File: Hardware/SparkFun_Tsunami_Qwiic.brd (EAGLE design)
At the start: 74.9 x 73.7 mm, 327 parts, among them J1 VDC-IN, J10 TRIG2, J11 TRIG1, J14 AUDIO I/O, J15 MIDI, J16 USB-C, J17 AGND, J2 GND-IN, J3 DEBUG, J4 QWIIC, J6 3.3VA, J7 3.3V, J8 PLAYING, J9 CORTEX_JTAG_DEBUG_PTH_NS, Q1 3.1A/30V/105mΩ, U1 LM1117, U3 ATSAMS70N20A-AN, U4 LMV324, U5 LM1117, U6 6N138M, U7 ADAU1328, U8 SN74AHC1G125, Y1 11.2896 MHz

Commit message: Single buffer gate change
drop in replacement for U8 single buffer IC, with new PROD_ID
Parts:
- U8: value SN74AHC1G125 -> 74AHC1G125W5-7
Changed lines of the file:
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@@
 <setting verticaltext="up"/>
 </settings>
-<grid distance="0.05" unitdist="inch" unit="inch" style="lines" multiple="1" display="yes" altdistance="0.001" altunitdist="inch" altunit="inch"/>
+<grid distance="0.05" unitdist="inch" unit="inch" style="lines" multiple="1" display="yes" altdistance="0.005" altunitdist="inch" altunit="inch"/>
 <layers>
 <layer number="1" name="Top" color="4" fill="1" visible="yes" active="yes"/>
@@
 <layer number="98" name="Guide" color="6" fill="1" visible="no" active="no"/>
 <layer number="99" name="SpiceOrder" color="7" fill="1" visible="no" active="no"/>
-<layer number="100" name="Muster" color="7" fill="1" visible="no" active="no"/>
+<layer number="100" name="Muster" color="7" fill="1" visible="no" active="yes"/>
 <layer number="101" name="Patch_Top" color="12" fill="4" visible="no" active="yes"/>
 <layer number="102" name="Vscore" color="7" fill="1" visible="no" active="yes"/>
@@
 <element name="U$94" library="output2" package="CIPO23" value="" x="39.375078125" y="40.15231875" smashed="yes" rot="MR270"/>
 <element name="U$95" library="output2" package="APDM26" value="" x="31.755078125" y="40.15231875" smashed="yes" rot="MR270"/>
-<element name="U8" library="SparkFun-IC-Logic" package="SOT23-5" value="SN74AHC1G125" x="26.416" y="59.944" smashed="yes">
+<element name="U8" library="SparkFun-IC-Logic" package="SOT23-5" value="74AHC1G125W5-7" x="26.416" y="59.944" smashed="yes">
 <attribute name="NAME" x="24.511" y="59.944" size="0.6096" layer="25" font="vector" ratio="20" rot="R90" align="bottom-center"/>
-<attribute name="PROD_ID" value="IC-11920" x="26.416" y="59.944" size="1.778" layer="27" font="vector" ratio="15" display="off"/>
-<attribute name="VALUE" x="28.956" y="59.944" size="0.6096" layer="27" font="vector" ratio="20" rot="R90" align="bottom-center"/>
+<attribute name="PROD_ID" value="IC-16588" x="26.416" y="59.944" size="1.778" layer="27" font="vector" ratio="15" display="off"/>
+<attribute name="VALUE" value="74AHC1G125W5-7" x="28.956" y="59.944" size="0.6096" layer="27" font="vector" ratio="20" rot="R90" align="bottom-center"/>
 </element>
 <element name="U5" library="SparkFun-IC-Power" package="SOT223" value="LM1117" x="53.34" y="40.386" smashed="yes" rot="R270">

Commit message: Swap 11MHz crystal for smaller package (3.2x2.5mm)
-also bumped version in bottom copper and SCH
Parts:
- Y1: device SparkFun-Clocks:CRYSTAL-OSC-SMD-5X3 -> SparkFun-Clocks:CRYSTAL-SMD-3.2X2.5MM_GEYER_12.60421
- moved C7 0.85 mm to (39.8, 22.2)
- moved C9 0.72 mm to (39.0, 28.6)
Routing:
- net N$1: track 10.0 -> 8.21 mm
- net N$2: track 6.94 -> 6.21 mm
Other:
- board text added: "V22"
- board text removed: "V21"
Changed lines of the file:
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@@
 <setting verticaltext="up"/>
 </settings>
-<grid distance="0.05" unitdist="inch" unit="inch" style="lines" multiple="1" display="yes" altdistance="0.005" altunitdist="inch" altunit="inch"/>
+<grid distance="0.05" unitdist="inch" unit="inch" style="lines" multiple="1" display="yes" altdistance="0.001" altunitdist="inch" altunit="inch"/>
 <layers>
 <layer number="1" name="Top" color="4" fill="1" visible="yes" active="yes"/>
@@
 <layer number="98" name="Guide" color="6" fill="1" visible="no" active="no"/>
 <layer number="99" name="SpiceOrder" color="7" fill="1" visible="no" active="no"/>
-<layer number="100" name="Muster" color="7" fill="1" visible="no" active="yes"/>
+<layer number="100" name="Muster" color="7" fill="1" visible="yes" active="yes"/>
 <layer number="101" name="Patch_Top" color="12" fill="4" visible="no" active="yes"/>
 <layer number="102" name="Vscore" color="7" fill="1" visible="no" active="yes"/>
@@
 <wire x1="0" y1="73.66" x2="0" y2="0" width="0.2032" layer="20"/>
 <text x="29.21" y="-31.75" size="1.778" layer="51" font="vector">Jamie Robertson &amp; Byron Jacquot</text>
-<text x="32.90061875" y="73.2663" size="1.778" layer="16" font="vector" ratio="15" rot="SMR180">V21</text>
+<text x="32.90061875" y="73.2663" size="1.778" layer="16" font="vector" ratio="15" rot="SMR180">V22</text>
 <wire x1="67.31" y1="71.12" x2="64.081659375" y2="71.137778125" width="0.2032" layer="21"/>
 <wire x1="63.573659375" y1="70.629778125" x2="64.081659375" y2="71.137778125" width="0.2032" layer="21"/>
@@
 <attribute name="REV" value="" x="-1.27" y="-31.75" size="1.778" layer="27" display="off"/>
 </element>
-<element name="C9" library="SparkFun-Capacitors" package="0402-TIGHT" value="12pF" x="38.686740625" y="29.220159375" smashed="yes">
-<attribute name="NAME" x="37.797740625" y="29.982159375" size="0.4064" layer="25" font="vector"/>
-<attribute name="PROD_ID" value="CAP-14665" x="38.686740625" y="29.220159375" size="1.778" layer="27" display="off"/>
-<attribute name="VALUE" x="37.670740625" y="28.077159375" size="0.4064" layer="27" font="vector"/>
-</element>
-<element name="C7" library="SparkFun-Capacitors" package="0402-TIGHT" value="12pF" x="39.22268125" y="21.529040625" smashed="yes" rot="R180">
-<attribute name="NAME" x="40.11168125" y="20.767040625" size="0.4064" layer="25" font="vector" rot="R180"/>
-<attribute name="PROD_ID" value="CAP-14665" x="39.22268125" y="21.529040625" size="1.778" layer="27" rot="R180" display="off"/>
-<attribute name="VALUE" x="40.23868125" y="22.672040625" size="0.4064" layer="27" font="vector" rot="R180"/>
+<element name="C9" library="SparkFun-Capacitors" package="0402-TIGHT" value="12pF" x="38.966140625" y="28.559759375" smashed="yes">
+<attribute name="NAME" x="38.077140625" y="29.321759375" size="0.4064" layer="25" font="vector"/>
+<attribute name="PROD_ID" value="CAP-14665" x="38.966140625" y="28.559759375" size="1.778" layer="27" display="off"/>
+<attribute name="VALUE" x="37.950140625" y="27.416759375" size="0.4064" layer="27" font="vector"/>
+</element>
+<element name="C7" library="SparkFun-Capacitors" package="0402-TIGHT" value="12pF" x="39.75608125" y="22.189440625" smashed="yes" rot="R180">
+<attribute name="NAME" x="40.64508125" y="21.427440625" size="0.4064" layer="25" font="vector" rot="R180"/>
+<attribute name="PROD_ID" value="CAP-14665" x="39.75608125" y="22.189440625" size="1.778" layer="27" rot="R180" display="off"/>
+<attribute name="VALUE" x="40.77208125" y="23.332440625" size="0.4064" layer="27" font="vector" rot="R180"/>
 </element>
 <element name="FB1" library="SparkFun-Coils" package="0603" value="470Ω" x="34.79291875" y="32.390078125" smashed="yes" rot="R270">
@@
 <attribute name="VALUE" value="0.1uF" x="61.468" y="51.054" size="0.4064" layer="27" font="vector" rot="R180"/>
 </element>
-<element name="Y1" library="SparkFun-Clocks" package="CRYSTAL-OSC-SMD-5X3" value="11.2896 MHz" x="39.37" y="25.4" smashed="yes" rot="R90">
-<attribute name="DKPART" value="887-2353-1-ND" x="39.37" y="25.4" size="1.778" layer="27" font="vector" ratio="15" rot="R90" display="off"/>
-<attribute name="MFR" value="txc" x="39.37" y="25.4" size="1.778" layer="27" font="vector" ratio="15" rot="R90" display="off"/>
-<attribute name="MFRPART" value="7B-11.2896MAAE-T" x="39.37" y="25.4" size="1.778" layer="27" font="vector" ratio="15" rot="R90" display="off"/>
+<element name="Y1" library="SparkFun-Clocks" package="CRYSTAL-SMD-3.2X2.5MM_GEYER_12.60421" value="11.2896 MHz" x="39.37" y="25.4" smashed="yes" rot="R90">
+<attribute name="MFR" value="GEYER" x="39.37" y="25.4" size="1.778" layer="27" font="vector" ratio="15" rot="R90" display="off"/>
+<attribute name="MODEL" value="KX-7T" x="39.37" y="25.4" size="1.778" layer="27" rot="R90" display="off"/>
+<attribute name="MRFPART" value="12.60421" x="39.37" y="25.4" size="1.778" layer="27" rot="R90" display="off"/>
 <attribute name="NAME" x="37.465" y="22.86" size="0.4064" layer="25" rot="R90"/>
-<attribute name="PROD_ID" value="XTAL-13463" x="39.37" y="25.4" size="1.778" layer="27" rot="R90" display="off"/>
+<attribute name="PROD_ID" value="XTAL-16991" x="39.37" y="25.4" size="1.778" layer="27" rot="R90" display="off"/>
 <attribute name="VALUE" x="41.91" y="22.86" size="0.4064" layer="27" rot="R90"/>
 </element>
@@
 <contactref element="C7" pad="1"/>
 <contactref element="U3" pad="98"/>
-<wire x1="34.57" y1="25.32" x2="39.958" y2="25.32" width="0.2032" layer="1"/>
-<wire x1="39.958" y1="25.32" x2="40.52" y2="24.758" width="0.2032" layer="1"/>
 <contactref element="Y1" pad="1"/>
-<wire x1="40.52" y1="23.55" x2="40.52" y2="24.758" width="0.2032" layer="1"/>
-<wire x1="39.72268125" y1="21.529040625" x2="40.23068125" y2="21.529040625" width="0.2032" layer="1"/>
-<wire x1="40.52" y1="21.818359375" x2="40.23068125" y2="21.529040625" width="0.2032" layer="1"/>
-<wire x1="40.52" y1="21.818359375" x2="40.52" y2="23.55" width="0.2032" layer="1"/>
+<wire x1="40.25608125" y1="22.189440625" x2="40.25608125" y2="24.23608125" width="0.2032" layer="1"/>
+<wire x1="40.25608125" y1="24.23608125" x2="40.27" y2="24.25" width="0.2032" layer="1"/>
+<wire x1="34.57" y1="25.32" x2="39.2" y2="25.32" width="0.2032" layer="1"/>
+<wire x1="39.2" y1="25.32" x2="40.27" y2="24.25" width="0.2032" layer="1"/>
 </signal>
 <signal name="N$2">
 <contactref element="C9" pad="1"/>
 <contactref element="U3" pad="99"/>
-<wire x1="34.57" y1="25.82" x2="38.012" y2="25.82" width="0.2032" layer="1"/>
 <contactref element="Y1" pad="3"/>
-<wire x1="38.22" y1="27.25" x2="38.22" y2="26.028" width="0.2032" layer="1"/>
-<wire x1="38.22" y1="26.028" x2="38.012" y2="25.82" width="0.2032" layer="1"/>
-<wire x1="38.186740625" y1="29.220159375" x2="38.186740625" y2="27.283259375" width="0.2032" layer="1"/>
-<wire x1="38.186740625" y1="27.283259375" x2="38.22" y2="27.25" width="0.2032" layer="1"/>
+<wire x1="38.47" y1="26.55" x2="38.466140625" y2="26.553859375" width="0.2032" layer="1"/>
+<wire x1="38.466140625" y1="26.553859375" x2="38.466140625" y2="28.559759375" width="0.2032" layer="1"/>
+<wire x1="34.57" y1="25.82" x2="37.74" y2="25.82" width="0.2032" layer="1"/>
+<wire x1="37.74" y1="25.82" x2="38.47" y2="26.55" width="0.2032" layer="1"/>
 </signal>
 <signal name="N$3">

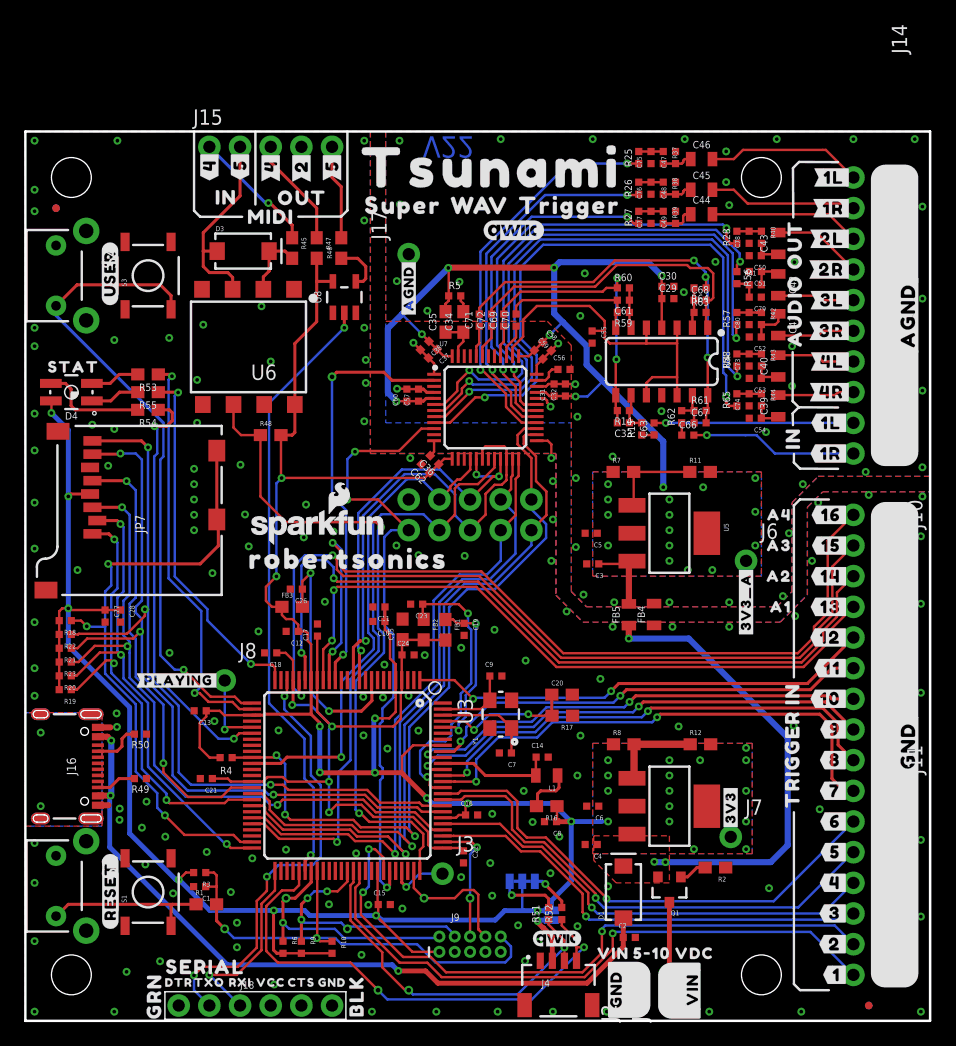
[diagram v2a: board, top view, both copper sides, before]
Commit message: Test points changed to larger size
-8 test points updated. Note, these used to be the small 15mil drill hit pth/via style test points. They are now the largest SMD pad style. Note, I also kept a via in the center point of all the test points, this was necessary to keep routing adjustments to a minimum and it will also help with pogo pin centering.
-Bumped version to v23 in BRD and both sheets of SCH
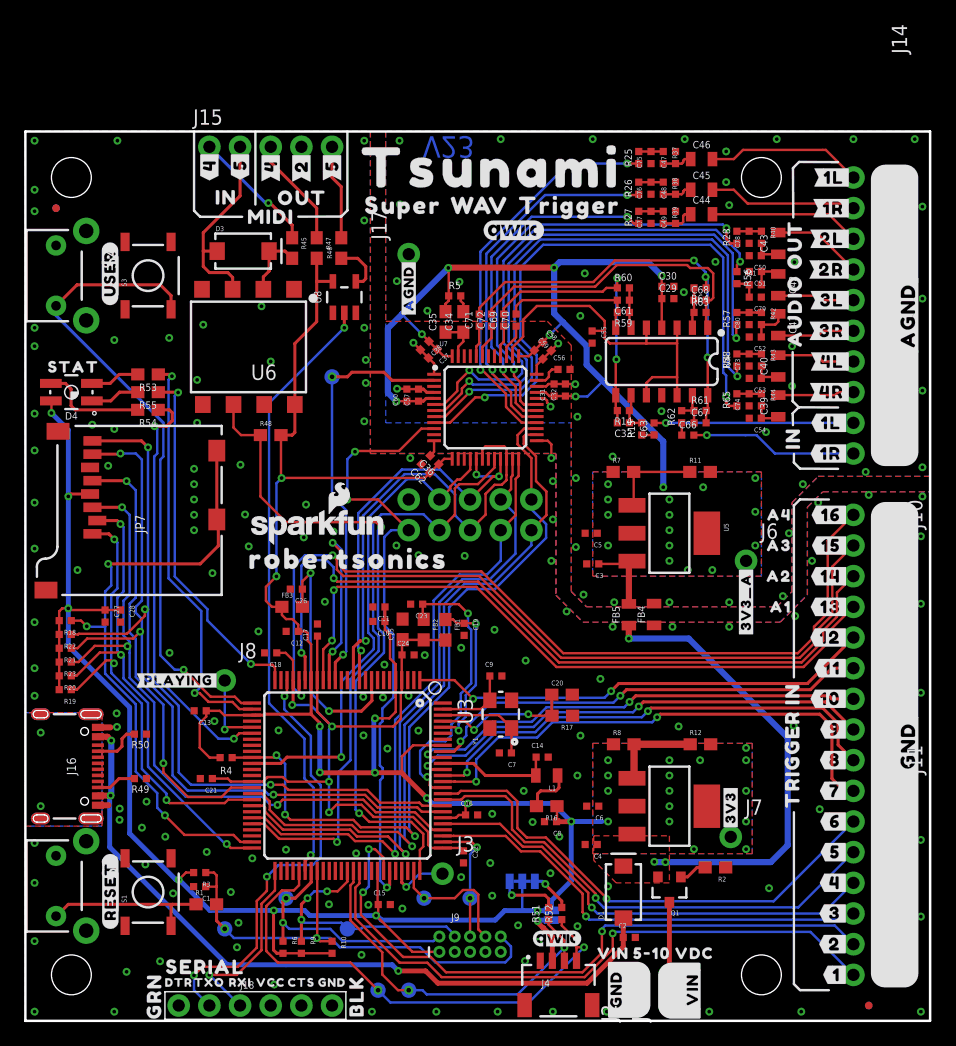
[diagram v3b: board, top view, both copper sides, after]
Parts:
- TP1, TP2, TP4, TP5, TP6, TP7, TP8, TP9: device SparkFun-Connectors:TP_15TH -> SparkFun-Connectors:PAD.03X.05
- flipped TP1 to the bottom
- flipped TP2 to the bottom
- flipped TP4 to the bottom
- flipped TP5 to the bottom
- flipped TP6 to the bottom
- flipped TP7 to the bottom
- flipped TP8 to the bottom
- flipped TP9 to the bottom
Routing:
- net I2C_SDA: track 30.7 -> 31.1 mm, vias 1 -> 2
- net SWDIO/TMS: track 20.8 -> 21.0 mm, vias 1 -> 2
- net I2C_SCK: track 42.6 -> 42.9 mm, vias 1 -> 2
- net NRESET: vias 1 -> 2
- net TDO: vias 1 -> 2
- net TDI: vias 0 -> 1
- net MCLK: vias 1 -> 2
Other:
- board text added: "V23"
- board text removed: "V22"
